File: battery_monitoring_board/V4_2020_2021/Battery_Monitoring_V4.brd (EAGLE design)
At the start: 57.1 x 161.5 mm, 120 parts, among them CON1 MOLEX_5566-2, CON2 SM03B-GHS-TB, CON3 SM03B-GHS-TB, J1 MKDS_5/2-6,352, J10 MKDS_5/2-6,352, J16 MKDS_5/2-6,352, J2 MKDS_5/2-6,352, J3 MKDS_5/2-6,352, J4 MKDS_5/2-6,352, J9 MKDS_5/2-6,352, Q1 TCLD1000CT, Q10 SI7145DP, Q11 SI7145DP, Q12 SI7145DP, Q13 SI7145DP, Q14 SI7145DP, Q15 PSMN1R5-30BLE, Q16 TCLD1000CT, Q17 NMOS-TO252, Q18 NMOS-TO252, Q19 NMOS-TO252, Q2 TCLD1000CT, Q20 NMOS-TO252, Q21 DMN2011UTS, Q3 TCLD1000CT, Q4 PSMN1R5-30BLE, Q5 PSMN1R5-30BLE, Q6 PSMN1R5-30BLE, Q7 SI7145DP, Q8 SI7145DP, Q9 SI7145DP, U1 INA3221., U10 LM5050-2, U12 IR2301S, U2 INA3221., U3 TEENSY_3.1_BASIC_2, U4 TCAN1042HVDR, U5 LTC4418, U6 LM5050-2, U7 LM5050-2, U8 LM5050-2

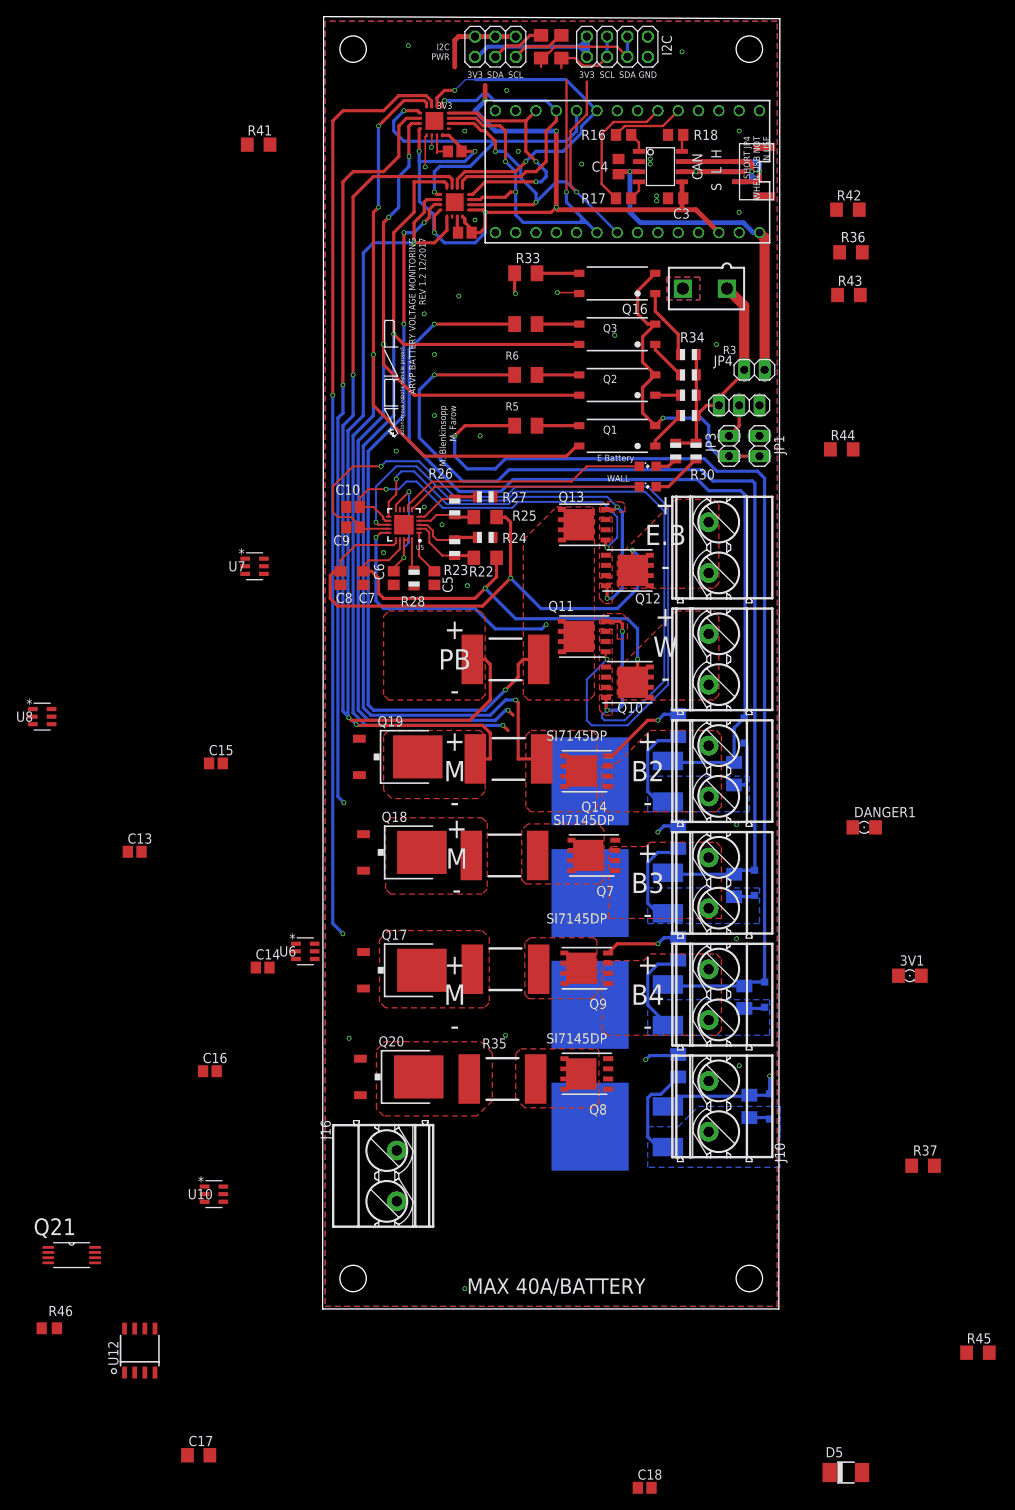
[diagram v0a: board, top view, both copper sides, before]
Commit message: renamed boards and fixed errors
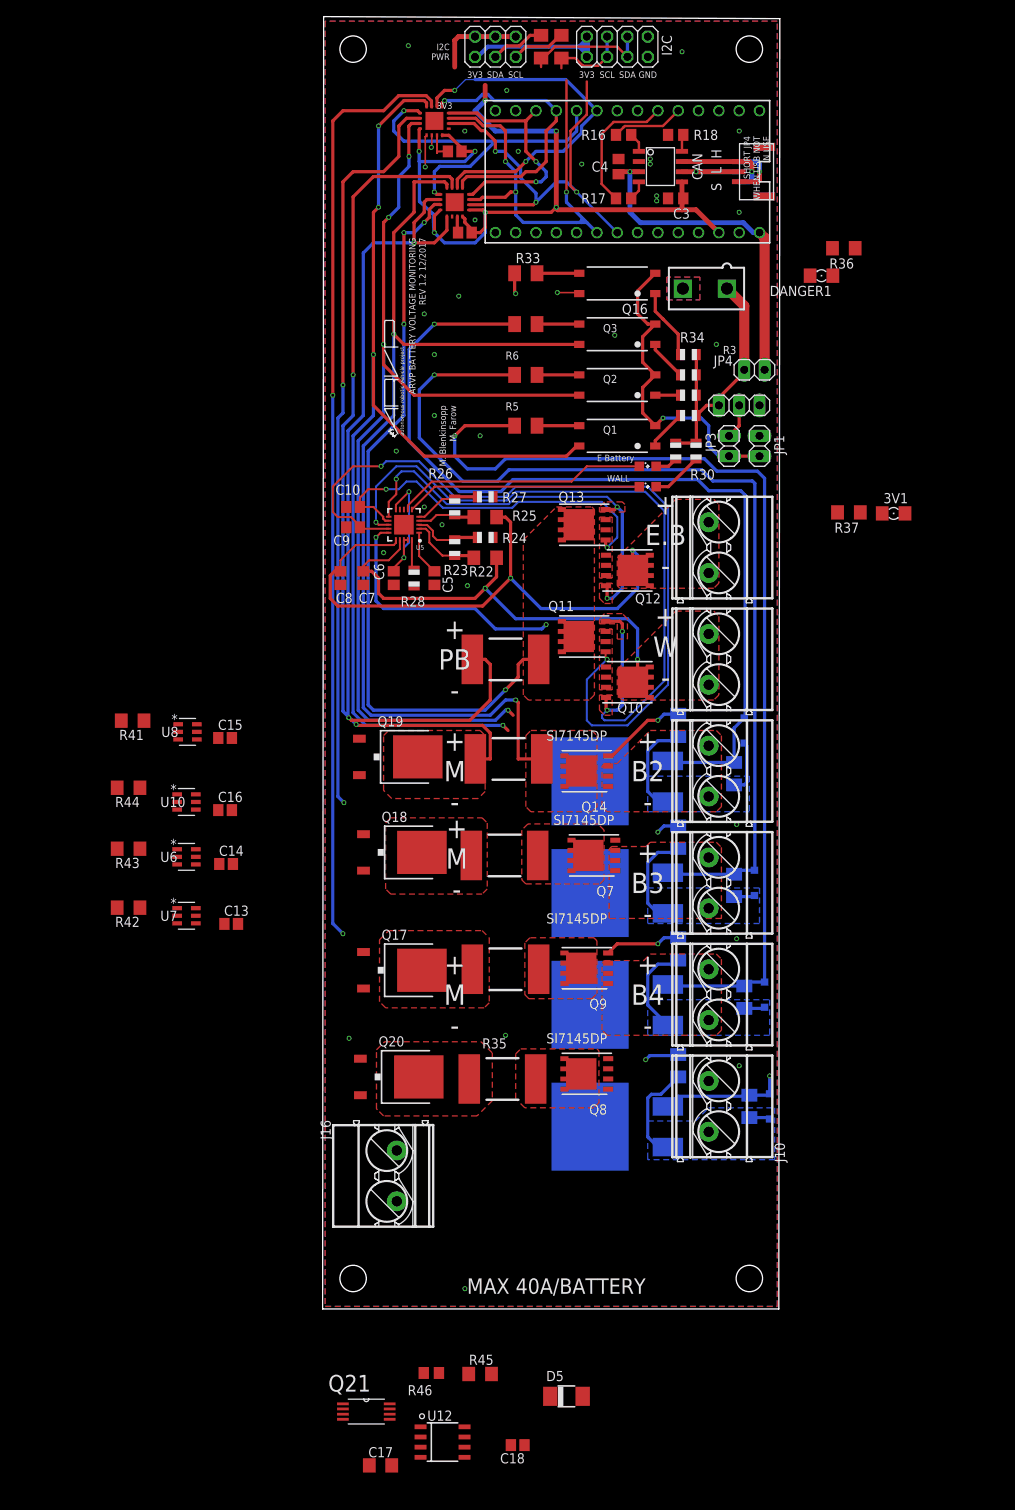
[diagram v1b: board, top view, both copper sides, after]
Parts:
- moved R42 125.3 mm to (-24.9, 50.8), turned to 180 degrees
- moved R43 113.6 mm to (-24.9, 58.2), turned to 180 degrees
- moved R44 98.7 mm to (-24.9, 65.8), turned to 180 degrees
- moved R37 82.2 mm to (65.2, 100.2), turned to 180 degrees
- moved R41 73.7 mm to (-24.4, 74.2), turned to 180 degrees
- moved DANGER1 69.2 mm to (61.7, 129.8), turned to 180 degrees
- moved R45 62.3 mm to (19.1, -7.49)
- moved 3V1 57.8 mm to (70.7, 100.1)
- moved U10 49.1 mm to (-17.7, 64.0)
- moved R46 48.1 mm to (13.0, -7.37), turned to 180 degrees
- moved U7 44.5 mm to (-17.7, 49.8)
- moved Q21 41.7 mm to (4.83, -12.2)
- moved U12 39.5 mm to (14.4, -16.0), turned to 270 degrees
- moved D5 36.2 mm to (29.8, -10.3)
- moved C16 32.7 mm to (-12.8, 63.0)
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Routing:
- removed copper zone on layer 1, net POWER_BOARD

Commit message: arranged power_board components
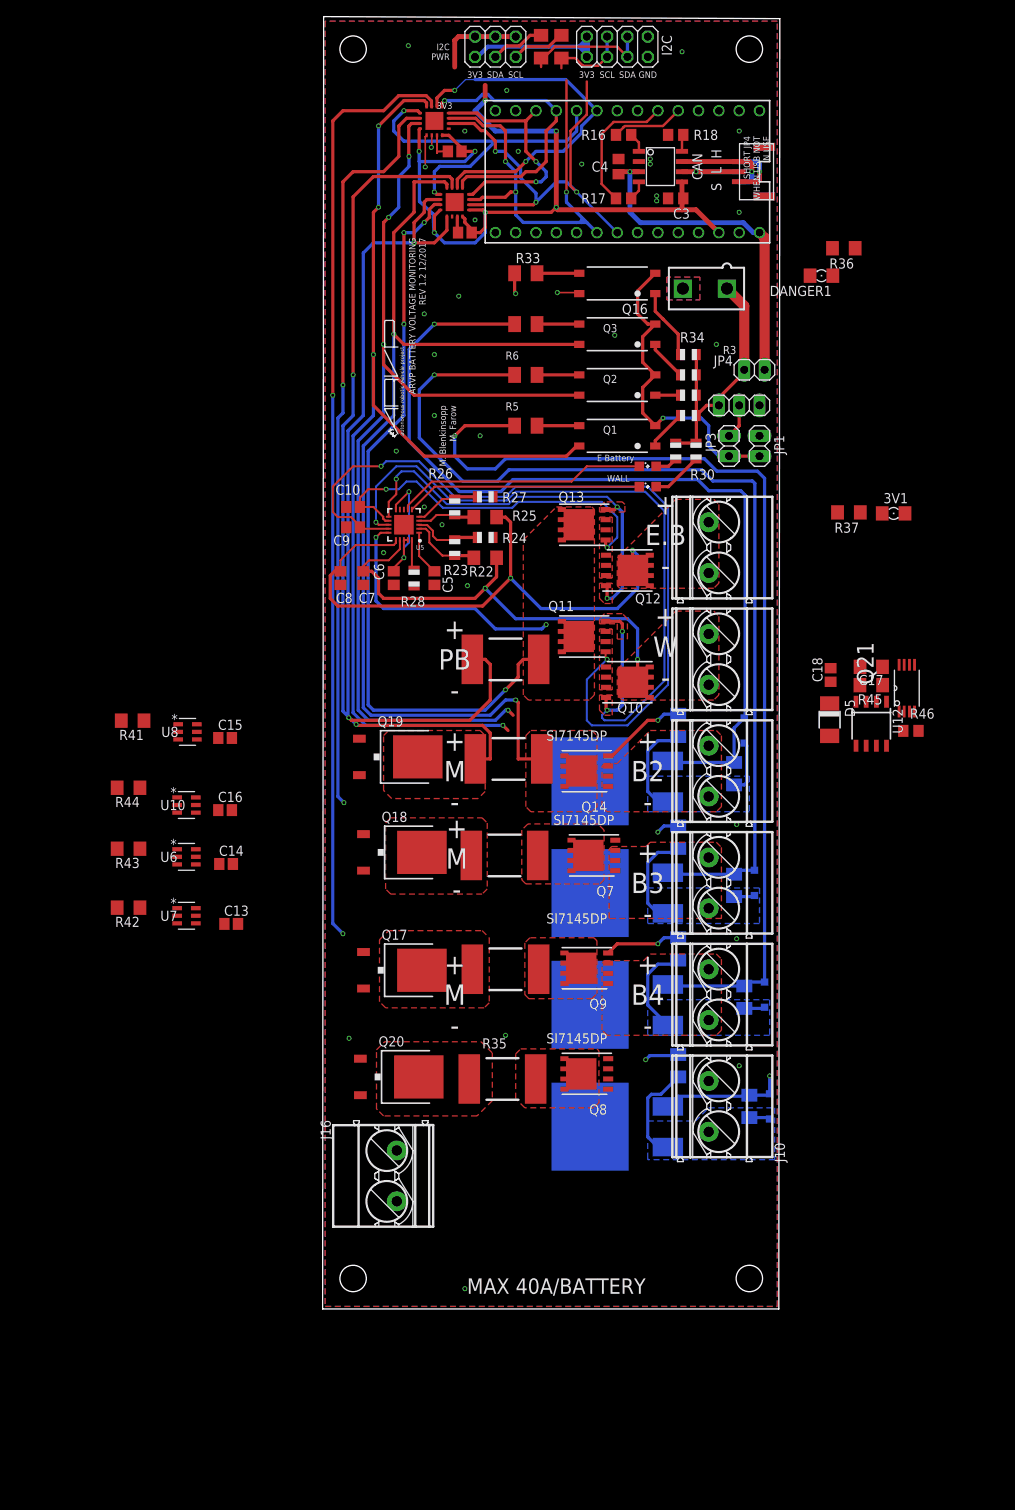
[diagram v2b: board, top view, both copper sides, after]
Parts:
- moved C17 117.2 mm to (67.9, 80.9), turned to 180 degrees
- moved Q21 112.9 mm to (72.4, 78.2), turned to 90 degrees
- moved U12 104.6 mm to (67.9, 73.8), turned to 180 degrees
- moved C18 103.9 mm to (62.9, 79.9), turned to 90 degrees
- moved R46 100.2 mm to (72.9, 72.9), turned to 0 degrees
- moved R45 99.0 mm to (67.9, 78.6), turned to 180 degrees
- moved D5 90.8 mm to (62.7, 74.3), turned to 270 degrees
- moved U10 0.38 mm to (-17.7, 63.6)

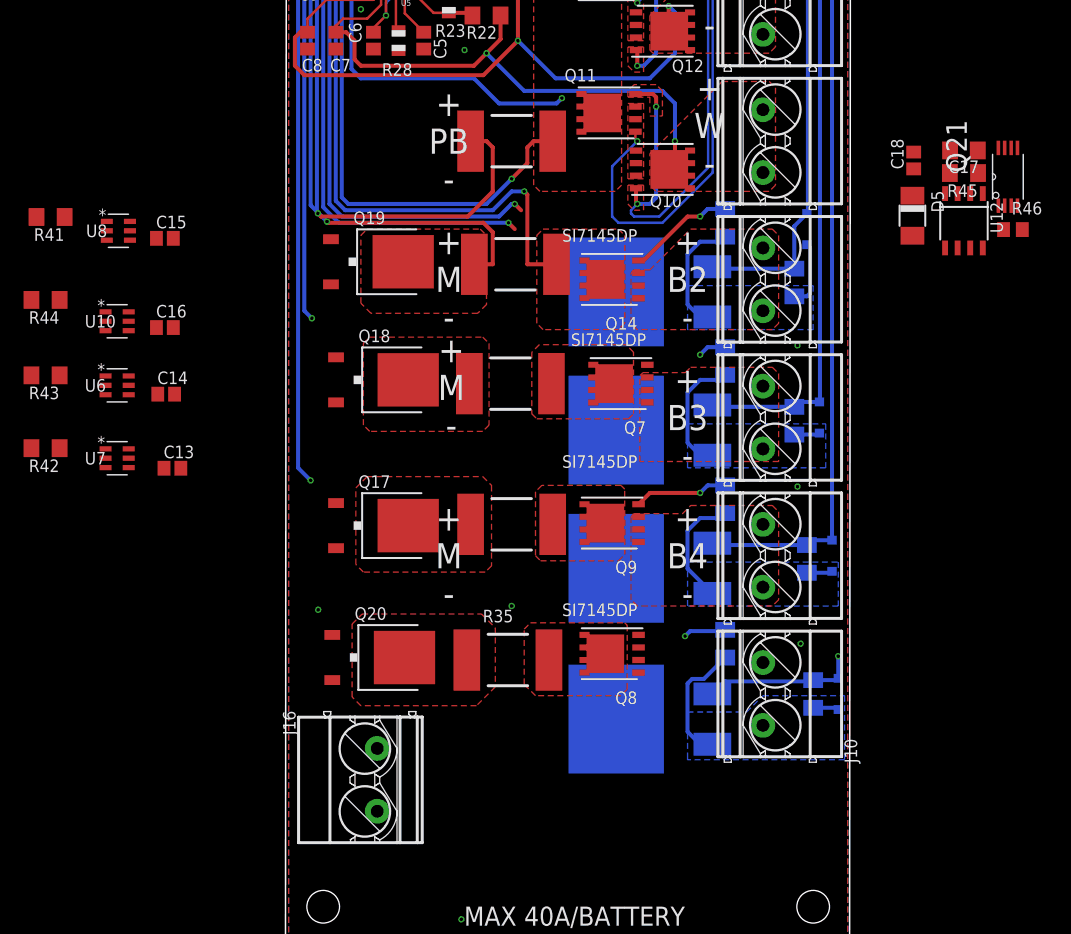
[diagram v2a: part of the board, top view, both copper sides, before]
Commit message: Minor adjustments to layout
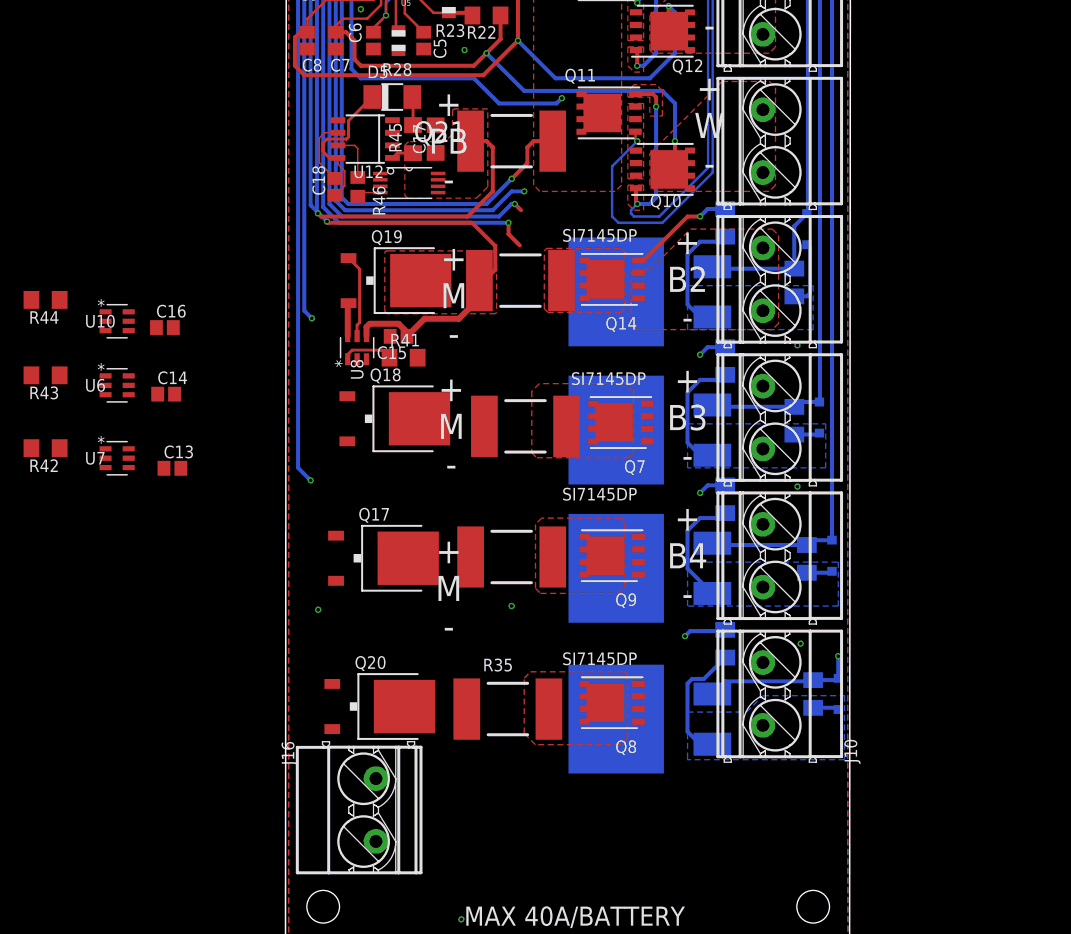
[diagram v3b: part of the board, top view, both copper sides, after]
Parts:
- moved R46 66.4 mm to (6.67, 77.2), turned to 270 degrees
- moved U12 61.1 mm to (7.43, 82.0), turned to 90 degrees
- moved Q21 60.5 mm to (11.9, 77.6), turned to 0 degrees
- moved C18 58.5 mm to (4.38, 77.2)
- moved R45 55.8 mm to (12.3, 82.0), turned to 90 degrees
- moved D5 53.9 mm to (10.2, 86.3), turned to 0 degrees
- moved C17 53.4 mm to (14.5, 82.0), turned to 90 degrees
- moved R41 38.4 mm to (11.3, 59.9), turned to 0 degrees
- moved U8 26.9 mm to (6.60, 61.0), turned to 90 degrees
- moved C15 25.6 mm to (10.8, 62.1), turned to 180 degrees
- moved Q20 4.95 mm to (8.89, 24.7)
- moved Q8 4.95 mm to (32.4, 25.1)
- moved R35 4.95 mm to (21.8, 24.4)
- moved R4 4.58 mm to (23.6, 53.0)
- moved Q18 4.10 mm to (10.4, 53.8)
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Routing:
- net MOTOR3: track 104.1 -> 121.0 mm
- net N$19: track 0.00 -> 15.4 mm
- net BATTERY_2: track 127.4 -> 117.0 mm
- net GATE3: track 0.00 -> 8.46 mm
- net N$18: track 0.00 -> 6.86 mm
- net N$9: track 9.55 -> 2.86 mm
- net IO4: track 0.00 -> 5.20 mm
- net GATE5: track 0.00 -> 5.04 mm
- net VOUT: track 0.00 -> 3.37 mm
- net N$21: track 0.00 -> 2.86 mm
- net N$20: track 0.00 -> 2.44 mm
- net POWER_BOARD: track 105.8 -> 108.1 mm
- net BATTERY_4: track 138.1 -> 139.9 mm
- added copper zone on layer 1, net POWER_BOARD
- removed copper zone on layer 1, net BATTERY3_IN
- removed copper zone on layer 1, net BATTERY4_IN
- removed copper zone on layer 1, net MOTOR2

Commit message: Component placement
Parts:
- moved R44 60.8 mm to (11.2, 16.9), turned to 0 degrees
- moved U10 51.7 mm to (6.48, 17.9), turned to 90 degrees
- moved C16 49.8 mm to (10.7, 19.1), turned to 180 degrees
- moved R43 45.0 mm to (11.2, 31.2), turned to 0 degrees
- moved R42 36.4 mm to (11.2, 45.6), turned to 0 degrees
- moved U6 34.6 mm to (6.48, 32.3), turned to 90 degrees
- moved C14 32.7 mm to (10.7, 33.4), turned to 180 degrees
- moved U7 24.3 mm to (6.48, 46.7), turned to 90 degrees
- moved C13 22.8 mm to (10.7, 47.8), turned to 180 degrees
- moved J16 16.3 mm to (24.1, 9.65), turned to 0 degrees
- moved Q20 1.52 mm to (10.4, 24.7)
- moved Q17 1.31 mm to (10.4, 39.0)
- moved R35 1.30 mm to (23.1, 24.7)
- moved R8 1.17 mm to (23.1, 39.0)
- moved Q9 1.02 mm to (32.9, 39.0)
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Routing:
- net MOTOR1: track 116.7 -> 133.5 mm
- net MOTOR2: track 93.3 -> 110.0 mm
- net MOTOR4: track 119.4 -> 135.9 mm
- net VOUT: track 3.37 -> 13.4 mm
- net GATE4: track 0.00 -> 8.56 mm
- net GATE1: track 0.00 -> 8.52 mm
- net GATE2: track 0.00 -> 8.48 mm
- net N$6: track 2.86 -> 10.6 mm
- net IO5: track 0.00 -> 5.27 mm
- net IO6: track 0.00 -> 5.20 mm
- net IO3: track 0.00 -> 5.00 mm
- removed copper zone on layer 1, net BATTERY2_IN
- removed copper zone on layer 1, net BATTERY_3
- removed copper zone on layer 1, net BATTERY_4
- removed copper zone on layer 1, net BATTERY_5
- removed copper zone on layer 1, net MOTOR1
- removed copper zone on layer 1, net MOTOR3
- removed copper zone on layer 1, net MOTOR4

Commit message: All components in place, beginning final tracing
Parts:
- moved 3V1 45.2 mm to (48.5, 139.4), turned to 270 degrees
- moved R37 43.6 mm to (46.1, 139.4), turned to 270 degrees
- moved DANGER1 20.4 mm to (41.5, 132.6)
- moved R36 18.0 mm to (46.5, 132.6)
- moved J16 4.04 mm to (28.2, 9.53)
- moved C3 1.65 mm to (41.8, 139.5)
- moved R16 1.65 mm to (35.3, 147.4)
- moved R17 1.65 mm to (35.3, 139.5)
- moved R18 1.65 mm to (41.8, 147.4)
- moved U4 1.65 mm to (39.9, 143.4)
- moved C4 1.65 mm to (34.7, 143.4)
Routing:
- net GND: track 5.77 -> 2.15 mm
- net CANL1: track 12.4 -> 16.0 mm
- net LED_D: track 0.00 -> 3.23 mm
- net N$23: track 0.00 -> 2.11 mm
- net CAN_TX_T: track 9.03 -> 10.8 mm
- net CANH1: track 12.6 -> 14.2 mm
- net CAN_RX_T: track 17.0 -> 18.7 mm
- net VIN: track 42.5 -> 43.1 mm
